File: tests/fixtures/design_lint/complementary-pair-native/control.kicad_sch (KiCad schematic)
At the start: 1 part, among them J1 Synthetic USB SuperSpeed conn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

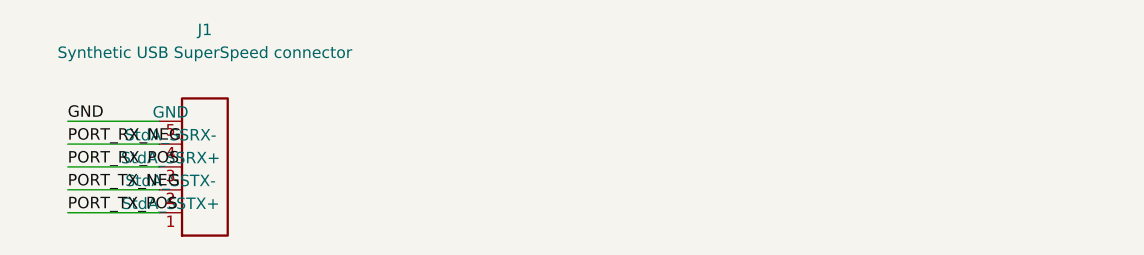
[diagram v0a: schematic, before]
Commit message: feat: recognize Ethernet complementary pair aliases
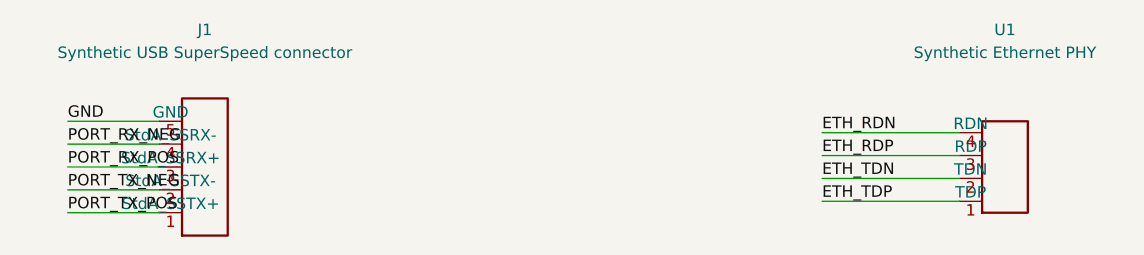
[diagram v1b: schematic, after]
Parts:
- added U1: Synthetic Ethernet PHY, Synthetic:EthernetPhy, symbol Synthetic:EthernetPhy
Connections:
- new net ETH_RDN: U1.4 (RDN)
- new net ETH_RDP: U1.3 (RDP)
- new net ETH_TDN: U1.2 (TDN)
- new net ETH_TDP: U1.1 (TDP)
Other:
- title: USB SuperSpeed pair control -> USB and Ethernet pair control
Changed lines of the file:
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@@
 (kicad_sch (version 20231120) (generator "eeschema")
   (paper "A4")
-  (title_block (title "USB SuperSpeed pair control")
+  (title_block (title "USB and Ethernet pair control")
     (comment 1 "NOT FOR MANUFACTURE - synthetic tooling fixture"))
   (symbol (lib_id "Synthetic:UsbSuperSpeedPort") (at 76.20 76.20 0) (unit 1)
@@
     (pin "4")
     (pin "5")
-    (instances (project "Synthetic USB SuperSpeed pair control" (path "/ddbbfff1-2dfd-5181-9d69-d3e7f697d99d" (reference "J1") (unit 1)))))
+    (instances (project "USB and Ethernet pair control" (path "/ddbbfff1-2dfd-5181-9d69-d3e7f697d99d" (reference "J1") (unit 1)))))
+  (symbol (lib_id "Synthetic:EthernetPhy") (at 165.10 76.20 0) (unit 1)
+    (in_bom yes) (on_board yes) (dnp no)
+    (property "Reference" "U1" (at 165.10 60.96 0) (effects (font (size 1.27 1.27))))
+    (property "Value" "Synthetic Ethernet PHY" (at 165.10 63.50 0) (effects (font (size 1.27 1.27))))
+    (property "Footprint" "Synthetic:EthernetPhy" (at 165.10 76.20 0) (effects (font (size 1.27 1.27)) hide))
+    (property "Datasheet" "" (at 165.10 76.20 0) (effects (font (size 1.27 1.27)) hide))
+    (pin "1")
+    (pin "2")
+    (pin "3")
+    (pin "4")
+    (instances (project "USB and Ethernet pair control" (path "/ddbbfff1-2dfd-5181-9d69-d3e7f697d99d" (reference "U1") (unit 1)))))
   (wire (pts (xy 71.12 81.28) (xy 60.96 81.28))
     (stroke (width 0) (type default))
@@
     (effects (font (size 1.27 1.27)) (justify left bottom))
 )
+  (wire (pts (xy 160.02 80.01) (xy 144.78 80.01))
+    (stroke (width 0) (type default)))
+  (wire (pts (xy 160.02 77.47) (xy 144.78 77.47))
+    (stroke (width 0) (type default)))
+  (wire (pts (xy 160.02 74.93) (xy 144.78 74.93))
+    (stroke (width 0) (type default)))
+  (wire (pts (xy 160.02 72.39) (xy 144.78 72.39))
+    (stroke (width 0) (type default)))
+  (label "ETH_TDP" (at 144.78 80.01 0)
+    (effects (font (size 1.27 1.27)) (justify left bottom))
+)
+  (label "ETH_TDN" (at 144.78 77.47 0)
+    (effects (font (size 1.27 1.27)) (justify left bottom))
+)
+  (label "ETH_RDP" (at 144.78 74.93 0)
+    (effects (font (size 1.27 1.27)) (justify left bottom))
+)
+  (label "ETH_RDN" (at 144.78 72.39 0)
+    (effects (font (size 1.27 1.27)) (justify left bottom))
+)

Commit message: test: isolate complementary pair native control
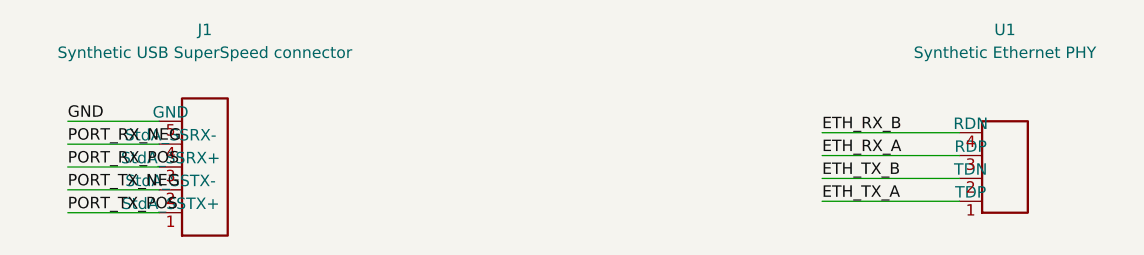
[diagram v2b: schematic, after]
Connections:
- net ETH_RDN renamed ETH_RX_B
- net ETH_RDP renamed ETH_RX_A
- net ETH_TDN renamed ETH_TX_B
- net ETH_TDP renamed ETH_TX_A
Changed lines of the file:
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@@
   (wire (pts (xy 160.02 72.39) (xy 144.78 72.39))
     (stroke (width 0) (type default)))
-  (label "ETH_TDP" (at 144.78 80.01 0)
+  (label "ETH_TX_A" (at 144.78 80.01 0)
     (effects (font (size 1.27 1.27)) (justify left bottom))
 )
-  (label "ETH_TDN" (at 144.78 77.47 0)
+  (label "ETH_TX_B" (at 144.78 77.47 0)
     (effects (font (size 1.27 1.27)) (justify left bottom))
 )
-  (label "ETH_RDP" (at 144.78 74.93 0)
+  (label "ETH_RX_A" (at 144.78 74.93 0)
     (effects (font (size 1.27 1.27)) (justify left bottom))
 )
-  (label "ETH_RDN" (at 144.78 72.39 0)
+  (label "ETH_RX_B" (at 144.78 72.39 0)
     (effects (font (size 1.27 1.27)) (justify left bottom))
 )
